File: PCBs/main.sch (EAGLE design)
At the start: 76 parts

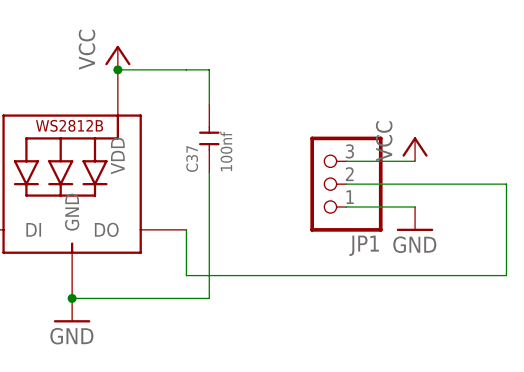
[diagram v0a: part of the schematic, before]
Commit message: reversed VCC/GND connections of LED PCB to simplify assembly
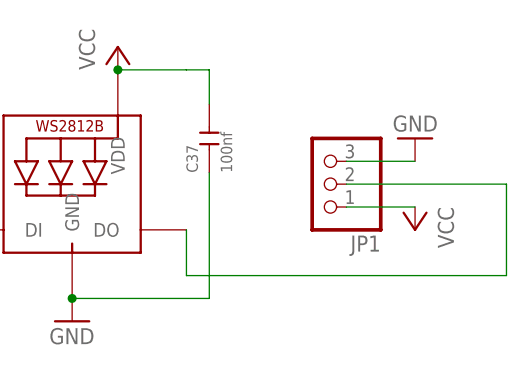
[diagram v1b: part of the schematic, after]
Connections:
- net GND: now also JP1.3; no longer JP1.1
- net VCC: now also JP1.1; no longer JP1.3
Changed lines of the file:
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@@
 <instance part="JP3" gate="A" x="0" y="45.72" rot="R180"/>
 <instance part="JP1" gate="A" x="1328.42" y="50.8" rot="R180"/>
-<instance part="GND39" gate="1" x="1338.58" y="45.72"/>
-<instance part="P+39" gate="VCC" x="1338.58" y="55.88"/>
+<instance part="GND39" gate="1" x="1338.58" y="55.88" rot="R180"/>
+<instance part="P+39" gate="VCC" x="1338.58" y="45.72" rot="R180"/>
 </instances>
 <busses>
@@
 </segment>
 <segment>
+<pinref part="JP1" gate="A" pin="1"/>
 <pinref part="P+39" gate="VCC" pin="VCC"/>
-<pinref part="JP1" gate="A" pin="3"/>
-<wire x1="1338.58" y1="53.34" x2="1330.96" y2="53.34" width="0.1524" layer="91"/>
+<wire x1="1330.96" y1="48.26" x2="1338.58" y2="48.26" width="0.1524" layer="91"/>
 </segment>
 </net>
@@
 </segment>
 <segment>
+<pinref part="JP1" gate="A" pin="3"/>
 <pinref part="GND39" gate="1" pin="GND"/>
-<pinref part="JP1" gate="A" pin="1"/>
-<wire x1="1338.58" y1="48.26" x2="1330.96" y2="48.26" width="0.1524" layer="91"/>
+<wire x1="1330.96" y1="53.34" x2="1338.58" y2="53.34" width="0.1524" layer="91"/>
 </segment>
 </net>
